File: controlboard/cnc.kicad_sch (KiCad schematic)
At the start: 20 parts, among them J2 LimitSwitch, J3 LimitSwitch, J4 LimitSwitch, J5 LimitSwitch, J6 Electromagnet/Servo, J7 Motor, J8 Motor, Q1 TODO, U2 ????

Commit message: more progress on controlboard pcb
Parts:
- added C6: C_Polarized, symbol Device:C_Polarized
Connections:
- net GND: now also C6.2
- net at JP2.2 (C), JP3.1 (A), Q1.3 (D): now also C6.1
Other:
- note added: "Our motors take 3.7ohm * 1A, 8W, worst case 16 prob + 12V 10 ohms = 1.2A for emag (oof, that's a lot LOT) so let's say 2A for the subsystem VMOT Nom: 10W motor, 6W emag with PWM -> 1.4A"
- note added: "~30 mA / on VIO pins"
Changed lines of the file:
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@@
+	)
+	(junction
+		(at 234.95 73.66)
+		(diameter 0)
+		(color 0 0 0 0)
 	)
 	(junction
@@
 	(wire
 		(pts
-			(xy 232.41 73.66) (xy 240.03 73.66)
+			(xy 232.41 73.66) (xy 234.95 73.66)
 		)
 		(stroke
@@
 	(wire
 		(pts
+			(xy 234.95 73.66) (xy 240.03 73.66)
+		)
+		(stroke
+			(width 0)
+			(type default)
+		)
+	)
+	(wire
+		(pts
 			(xy 87.63 137.16) (xy 90.17 137.16)
 		)
@@
 		(exclude_from_sim no)
 		(at 192.278 65.278 0)
+		(effects
+			(font
+				(size 1.27 1.27)
+			)
+		)
+	)
+	(text "Our motors take 3.7ohm * 1A, 8W, worst case 16 prob\n+ 12V 10 ohms = 1.2A for emag (oof, that's a lot LOT)\n\nso let's say 2A for the subsystem VMOT\n\nNom: 10W motor, 6W emag with PWM -> 1.4A"
+		(exclude_from_sim no)
+		(at 78.232 162.306 0)
+		(effects
+			(font
+				(size 1.27 1.27)
+			)
+		)
+	)
+	(text "~30 mA / on VIO pins\n"
+		(exclude_from_sim no)
+		(at 78.486 154.178 0)
 		(effects
 			(font
@@
 	)
 	(symbol
+		(lib_id "Device:C_Polarized")
+		(at 234.95 77.47 0)
+		(unit 1)
+		(exclude_from_sim no)
+		(in_bom yes)
+		(on_board yes)
+		(dnp no)
+		(property "Reference" "C6"
+			(at 235.712 80.518 0)
+			(effects
+				(font
+					(size 1.27 1.27)
+				)
+				(justify left)
+			)
+		)
+		(property "Value" "C_Polarized"
+			(at 238.76 77.8509 0)
+			(effects
+				(font
+					(size 1.27 1.27)
+				)
+				(justify left)
+				(hide yes)
+			)
+		)
+		(property "Footprint" ""
+			(at 235.9152 81.28 0)
+			(effects
+				(font
+					(size 1.27 1.27)
+				)
+				(hide yes)
+			)
+		)
+		(property "Datasheet" "~"
+			(at 234.95 77.47 0)
+			(effects
+				(font
+					(size 1.27 1.27)
+				)
+				(hide yes)
+			)
+		)
+		(property "Description" "Polarized capacitor"
+			(at 234.95 77.47 0)
+			(effects
+				(font
+					(size 1.27 1.27)
+				)
+				(hide yes)
+			)
+		)
+		(pin "2"
+		)
+		(pin "1"
+		)
+		(instances
+			(project "controlboard"
+				(path "/2797250d-6fee-4769-b4dd-0e20ce4f0941/5be4ea58-2822-4c96-82fa-ac7323f92cc7"
+					(reference "C6")
+					(unit 1)
+				)
+			)
+		)
+	)
+	(symbol
 		(lib_id "power:GND")
 		(at 90.17 90.17 0)
@@
 					(unit 1)
 				)
+			)
+		)
+	)
+	(symbol
+		(lib_id "power:GND")
+		(at 234.95 81.28 0)
+		(unit 1)
+		(exclude_from_sim no)
+		(in_bom yes)
+		(on_board yes)
+		(dnp no)
+		(fields_autoplaced yes)
+		(property "Reference" "#PWR025"
+			(at 234.95 87.63 0)
+			(effects
+				(font
+					(size 1.27 1.27)
+				)
+				(hide yes)
+			)
+		)
+		(property "Value" "GND"
+			(at 234.95 86.36 0)
+			(effects
+				(font
+					(size 1.27 1.27)
+				)
+				(hide yes)
+			)
+		)
+		(property "Footprint" ""
+			(at 234.95 81.28 0)
+			(effects
+				(font
+					(size 1.27 1.27)
+				)
+				(hide yes)
+			)
+		)
+		(property "Datasheet" ""
+			(at 234.95 81.28 0)
+			(effects
+				(font
+					(size 1.27 1.27)
+				)
+				(hide yes)
+			)
+		)
+		(property "Description" ""
+			(at 234.95 81.28 0)
+			(effects
+				(font
+					(size 1.27 1.27)
+				)
+				(hide yes)
+			)
+		)
+		(pin "1"
+		)
+		(instances
+			(project "controlboard"
+				(path "/2797250d-6fee-4769-b4dd-0e20ce4f0941/5be4ea58-2822-4c96-82fa-ac7323f92cc7"
+					(reference "#PWR025")
+					(unit 1)
+				)

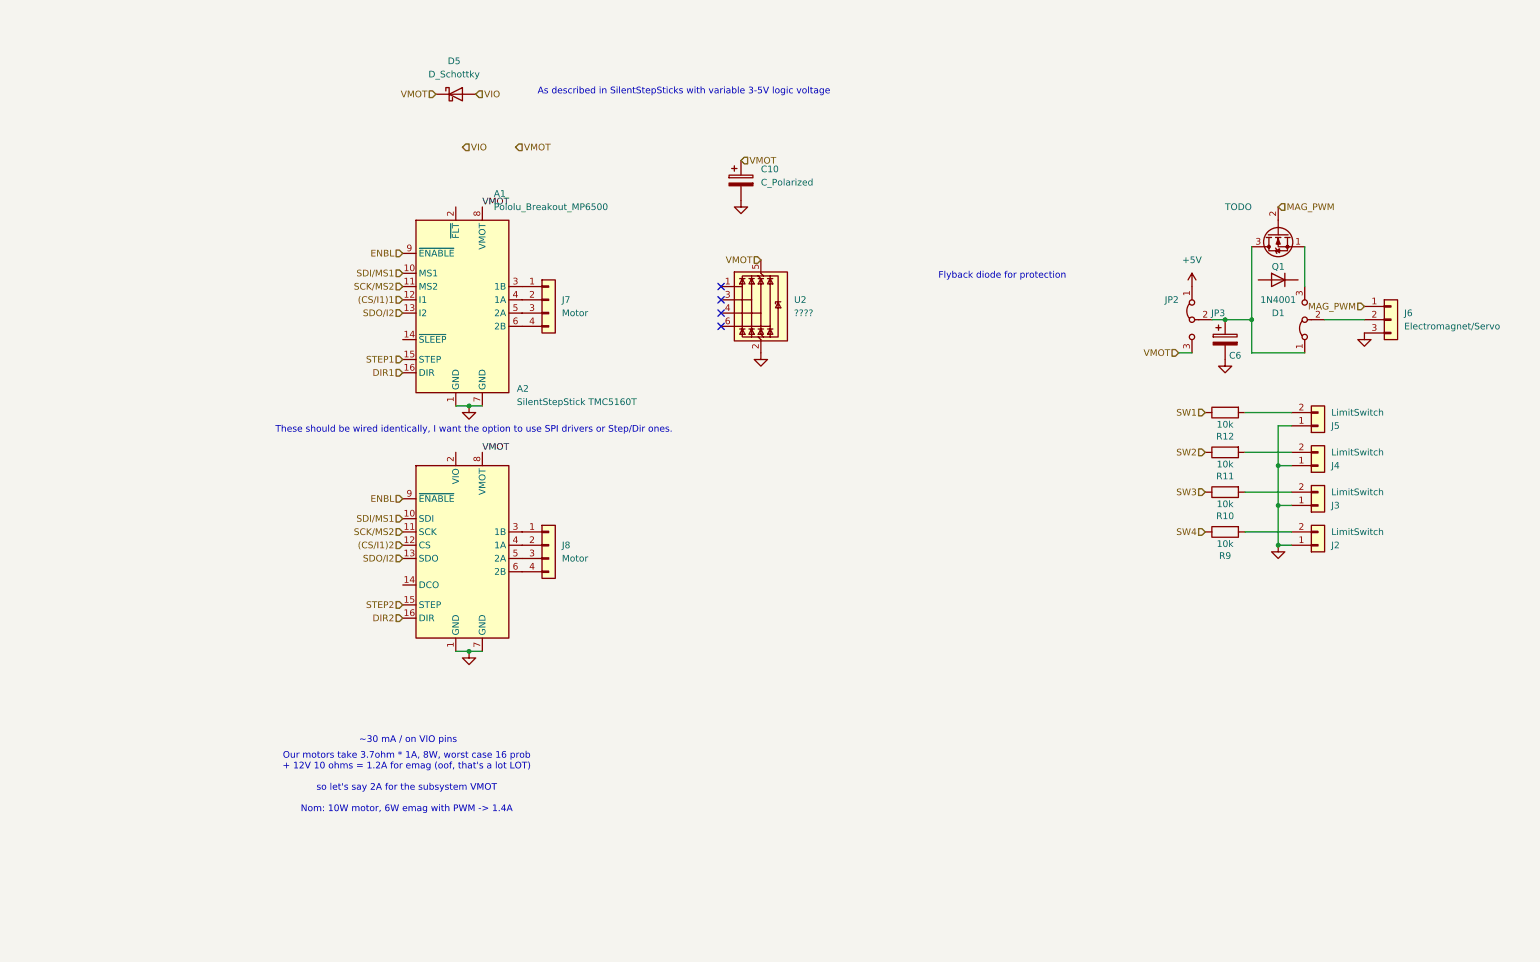
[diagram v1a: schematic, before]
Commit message: ControlBoard Schematic nearly done
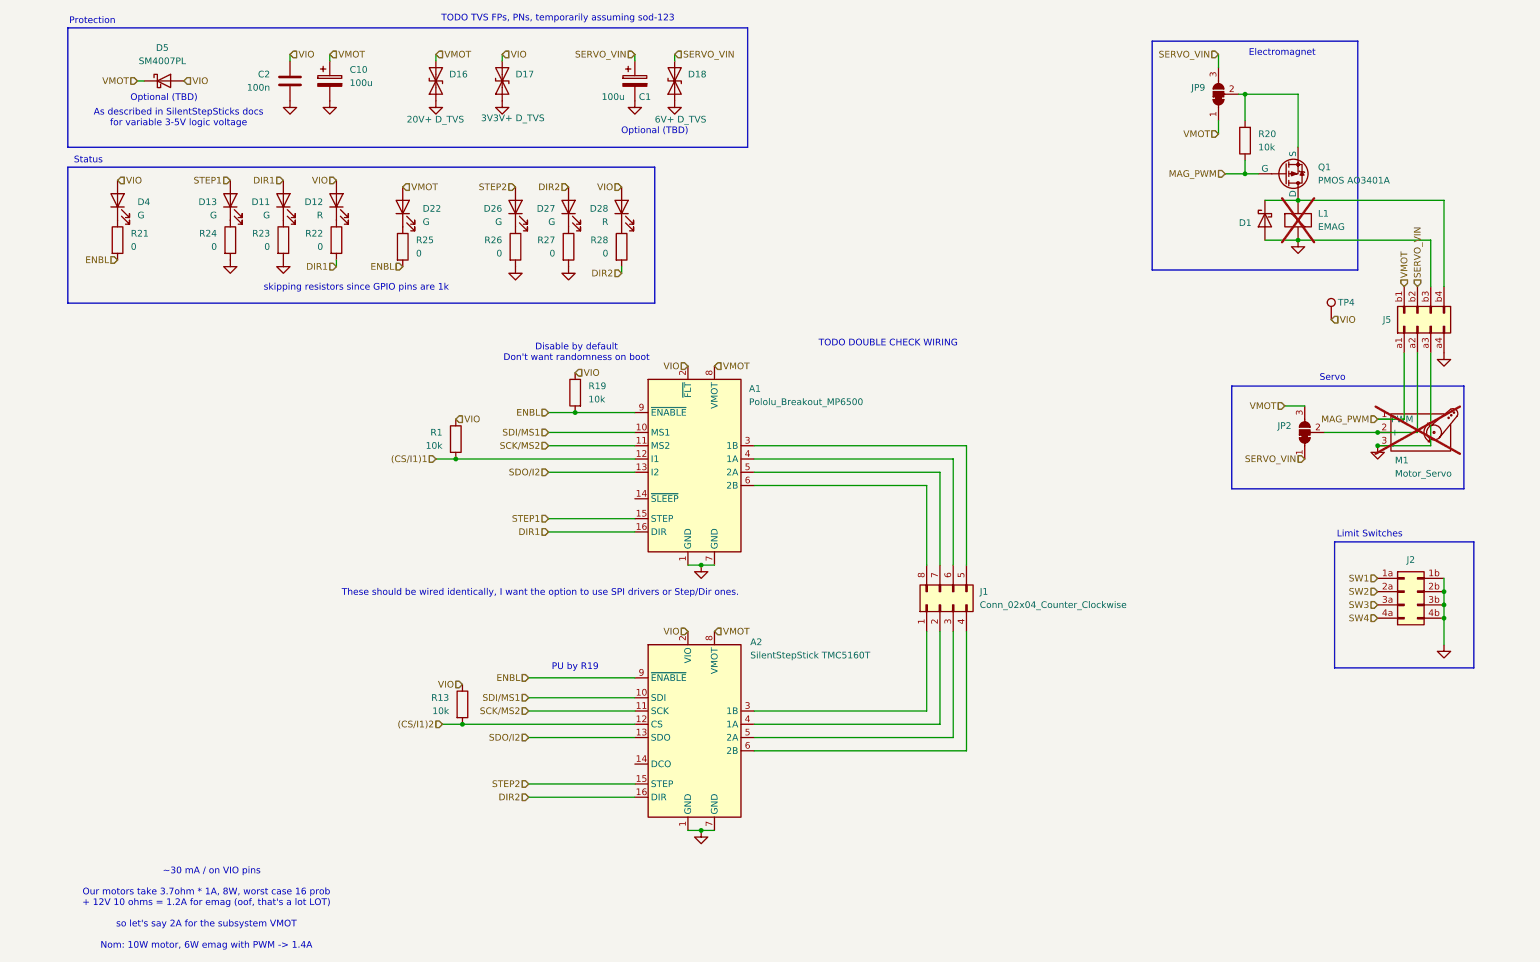
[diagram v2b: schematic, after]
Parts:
- removed C6: C_Polarized, symbol Device:C_Polarized
- removed D1: 1N4001, Diode_THT:D_DO-41_SOD81_P10.16mm_Horizontal, symbol Diode:1N4001
- removed J2, J3, J4, J5: LimitSwitch, symbol Connector_Generic:Conn_01x02
- removed J6: Electromagnet/Servo, symbol Connector_Generic:Conn_01x03
- removed J7, J8: Motor, symbol Connector_Generic:Conn_01x04
- removed JP2, JP3: Jumper_3_Bridged12, symbol Jumper:Jumper_3_Bridged12
- removed Q1: TODO, Package_TO_SOT_THT:TO-92_Inline, symbol Transistor_FET:2N7000
- removed R10, R11, R12, R9: 10k, symbol Device:R
- removed U2: ????, Package_TO_SOT_SMD:SOT-23-6, symbol Power_Protection:WE-TVS-824015043
- added C1: 100u, Capacitor_SMD:CP_Elec_6.3x5.4, symbol Device:C_Polarized
- added C2: 100n, Capacitor_SMD:C_0603_1608Metric_Pad1.08x0.95mm_HandSolder, symbol Device:C
- added D1: SM4007PL, Diode_SMD:Nexperia_CFP3_SOD-123W, symbol Device:D_Schottky
- added D11, D13, D22, D26, D27, D4: G, LED_SMD:LED_0603_1608Metric_Pad1.05x0.95mm_HandSolder, symbol Device:LED
- added D12, D28: R, LED_SMD:LED_0603_1608Metric_Pad1.05x0.95mm_HandSolder, symbol Device:LED
- added D16: 20V+ D_TVS, Diode_SMD:D_SOD-123F, symbol Device:D_TVS
- added D17: 3V3V+ D_TVS, Diode_SMD:D_SOD-123F, symbol Device:D_TVS
- added D18: 6V+ D_TVS, Diode_SMD:D_SOD-123F, symbol Device:D_TVS
- added J1: Conn_02x04_Counter_Clockwise, Connector_PinSocket_2.54mm:PinSocket_2x04_P2.54mm_Horizontal, symbol Connector_Generic:Conn_02x04_Counter_Clockwise
- added J2: Conn_02x04_Row_Letter_Last, Connector_PinSocket_2.54mm:PinSocket_2x04_P2.54mm_Horizontal, symbol Connector_Generic:Conn_02x04_Row_Letter_Last
- added J5: Conn_02x04_Row_Letter_First, Connector_PinSocket_2.54mm:PinSocket_2x04_P2.54mm_Horizontal, symbol Connector_Generic:Conn_02x04_Row_Letter_First
- added JP2, JP9: SolderJumper_3_Bridged12, Jumper:SolderJumper-3_P1.3mm_Bridged12_RoundedPad1.0x1.5mm, symbol Jumper:SolderJumper_3_Bridged12
- added L1: EMAG, symbol Device:ElectromagneticActor
- added M1: Motor_Servo, symbol Motor:Motor_Servo
- added Q1: PMOS AO3401A, Package_TO_SOT_SMD:SOT-23_Handsoldering, symbol Simulation_SPICE:PMOS
- added R1, R13, R19, R20: 10k, Resistor_SMD:R_0603_1608Metric_Pad0.98x0.95mm_HandSolder, symbol Device:R
- added R21, R22, R23, R24, R25, R26, R27, R28: 0, Resistor_SMD:R_0603_1608Metric_Pad0.98x0.95mm_HandSolder, symbol Device:R
- added TP4: TestPoint, Connector_PinSocket_2.54mm:PinSocket_1x01_P2.54mm_Vertical, symbol Connector:TestPoint
- C10: value C_Polarized -> 100u; footprint (none) -> Capacitor_SMD:CP_Elec_6.3x5.4
- D5: value D_Schottky -> SM4007PL; footprint (none) -> Diode_SMD:Nexperia_CFP3_SOD-123W
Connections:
- net (CS/I1)1: now also R1.2
- net (CS/I1)2: now also R13.2
- net DIR1: now also D11.2 (A), R22.2
- net DIR2: now also D27.2 (A), R28.2
- net ENBL: now also R19.2, R21.2, R25.2
- net GND: now also C1.2, C2.2, D1.2 (A), D16.1 (A1), D17.1 (A1), D18.1 (A1), J2.1b (Pin_1b), J2.2b (Pin_2b), J2.3b (Pin_3b), J2.4b (Pin_4b), J5.a3 (Pin_a3), J5.a4 (Pin_a4), J5.b3 (Pin_b3), L1.2 (+), M1.3 (-), R23.2, R24.2, R26.2, R27.2
- net MAG_PWM: now also J5.a1 (Pin_a1), M1.1 (PWM), Q1.2 (G), R20.1
- net STEP1: now also D13.2 (A)
- net STEP2: now also D26.2 (A)
- net SW1: now also J2.1a (Pin_1a)
- net SW2: now also J2.2a (Pin_2a)
- net SW3: now also J2.3a (Pin_3a)
- net SW4: now also J2.4a (Pin_4a)
- net VIO: now also A1.2 (~{FLT}), A2.2 (VIO), C2.1, D12.2 (A), D17.2 (A2), D28.2 (A), D4.2 (A), R1.1, R13.1, R19.1, TP4.1
- net VMOT: now also D16.2 (A2), D22.2 (A), J5.b1 (Pin_b1), JP2.3 (B), JP9.1 (A)
- net at A2.3 (1B): now also J1.1 (Pin_1)
- net at A2.4 (1A): now also J1.2 (Pin_2)
- net at A2.5 (2A): now also J1.3 (Pin_3)
- net at A2.6 (2B): now also J1.4 (Pin_4)
- net at A1.3 (1B): now also J1.5 (Pin_5)
- net at A1.4 (1A): now also J1.6 (Pin_6)
- net at A1.5 (2A): now also J1.7 (Pin_7)
- net at A1.6 (2B): now also J1.8 (Pin_8)
- new net: D26.1 (K), R26.1
- new net: D22.1 (K), R25.1
- new net: D28.1 (K), R28.1
- new net: D13.1 (K), R24.1
- new net: J5.a2 (Pin_a2), JP2.2 (C), M1.2 (+)
- new net: D4.1 (K), R21.1
- new net: D1.1 (K), J5.b4 (Pin_b4), L1.1 (-), Q1.1 (D)
- new net: D12.1 (K), R22.1
- new net: D27.1 (K), R27.1
- new net: JP9.2 (C), Q1.3 (S), R20.2
- new net: D11.1 (K), R23.1
- new net SERVO_VIN: C1.1, D18.2 (A2), J5.b2 (Pin_b2), JP2.1 (A), JP9.3 (B)
- no-connect marks 4 -> 0
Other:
- note added: "As described in SilentStepSticks docs for variable 3-5V logic voltage"
- note added: "Disable by default Don't want randomness on boot"
- note added: "Electromagnet"
- note added: "Limit Switches"
- note added: "Optional (TBD)"
- note added: "PU by R19"
- note added: "Protection"
- note added: "Servo"
- note added: "Status"
- note added: "TODO DOUBLE CHECK WIRING"
- note added: "TODO TVS FPs, PNs, temporarily assuming sod-123"
- note added: "skipping resistors since GPIO pins are 1k"
- note removed: "As described in SilentStepSticks with variable 3-5V logic voltage"
- note removed: "Flyback diode for protection"
- moved on the sheet: A1, A2, C10, D5

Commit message: schematic improvements
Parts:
- removed D22: G, LED_SMD:LED_0603_1608Metric_Pad1.05x0.95mm_HandSolder, symbol Device:LED
- removed R21, R22, R23, R24, R25, R26, R27, R28: 0, Resistor_SMD:R_0603_1608Metric_Pad0.98x0.95mm_HandSolder, symbol Device:R
- D4: value G -> Y
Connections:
- net DIR1: now also D12.1 (K)
- net DIR2: now also D28.1 (K)
- net ENBL: now also D4.1 (K)
- net GND: now also D11.1 (K), D13.1 (K), D26.1 (K), D27.1 (K)
- net VIO: now also J5.b1 (Pin_b1); no longer TP4.1
- net VMOT: now also TP4.1; no longer J5.b1 (Pin_b1)
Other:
- note added: "Assuming sod-123 TVS, will select part numbers later"
- note added: "TODO DOUBLE CHECK THAT PINOUT/SYMBOL/WIRING IS CORRECT FOR MP6500 POLOLU"
- note added: "TODO: Double check that all GPIO pins used by LEDs have resistors (pretty sure they do)"
- note added: "TODO: is this circuit correct"
- note added: "Using software pullups"
- note removed: "TODO DOUBLE CHECK WIRING"
- note removed: "TODO TVS FPs, PNs, temporarily assuming sod-123"

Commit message: erc should be good now
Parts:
- A1: symbol chessbot-parts:Pololu_Breakout_MP6500 -> 0chessbot-parts:Pololu_Breakout_MP6500
- A2: symbol chessbot-parts:SilentStepStick -> 0chessbot-parts:SilentStepStick
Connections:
- no-connect marks 0 -> 2

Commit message: pcb layout work
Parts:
- J2: symbol Connector_Generic:Conn_02x04_Row_Letter_Last -> Connector_Generic:Conn_02x04_Odd_Even
- J5: symbol Connector_Generic:Conn_02x04_Row_Letter_First -> Connector_Generic:Conn_02x04_Odd_Even
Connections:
- net GND: now also J2.2 (Pin_2), J2.4 (Pin_4), J2.6 (Pin_6), J2.8 (Pin_8), J5.5 (Pin_5), J5.6 (Pin_6), J5.7 (Pin_7); no longer J2.1b (Pin_1b), J2.2b (Pin_2b), J2.3b (Pin_3b), J2.4b (Pin_4b), J5.a3 (Pin_a3), J5.a4 (Pin_a4), J5.b3 (Pin_b3)
- net MAG_PWM: now also J5.1 (Pin_1); no longer J5.a1 (Pin_a1)
- net SERVO_VIN: now also J5.4 (Pin_4); no longer J5.b2 (Pin_b2)
- net SW1: now also J2.1 (Pin_1); no longer J2.1a (Pin_1a)
- net SW2: now also J2.3 (Pin_3); no longer J2.2a (Pin_2a)
- net SW3: now also J2.5 (Pin_5); no longer J2.3a (Pin_3a)
- net SW4: now also J2.7 (Pin_7); no longer J2.4a (Pin_4a)
- net VIO: now also J5.2 (Pin_2); no longer J5.b1 (Pin_b1)
- net at JP2.2 (C), M1.2 (+): now also J5.3 (Pin_3); no longer J5.a2 (Pin_a2)
- net at D1.1 (K), L1.1 (-), Q1.1 (D): now also J5.8 (Pin_8); no longer J5.b4 (Pin_b4)

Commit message: progress
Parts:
- removed C1: 100u, Capacitor_SMD:CP_Elec_6.3x5.4, symbol Device:C_Polarized
- removed J1: Conn_02x04_Counter_Clockwise, Connector_PinSocket_2.54mm:PinSocket_2x04_P2.54mm_Horizontal, symbol Connector_Generic:Conn_02x04_Counter_Clockwise
- added C1: 22uF, Capacitor_SMD:C_1206_3216Metric_Pad1.33x1.80mm_HandSolder, symbol Device:C
- added D9: 20V+ D_TVS, Diode_SMD:D_SOD-123F, symbol Device:D_TVS
- added J1: Conn_02x04_Counter_Clockwise, Connector_PinSocket_2.54mm:PinSocket_2x04_P2.54mm_Horizontal, symbol Connector_Generic:Conn_02x04_Odd_Even
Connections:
- net GND: now also C1.2, D9.1 (A1)
- net SERVO_VIN: now also C1.1
- net VMOT: now also D9.2 (A2)
- net at A2.3 (1B): now also J1.2 (Pin_2)
- net at A2.4 (1A): now also J1.4 (Pin_4)
- net at A2.5 (2A): now also J1.6 (Pin_6)
- net at A2.6 (2B): now also J1.8 (Pin_8)
- net at A1.3 (1B): now also J1.1 (Pin_1)
- net at A1.4 (1A): now also J1.3 (Pin_3)
- net at A1.5 (2A): now also J1.5 (Pin_5)
- net at A1.6 (2B): now also J1.7 (Pin_7)
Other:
- moved on the sheet: D11, D12, D13, D26, D27, D28, D4

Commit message: yay its all connected
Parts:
- TP4: footprint Connector_PinSocket_2.54mm:PinSocket_1x01_P2.54mm_Vertical -> TestPoint:TestPoint_THTPad_D2.0mm_Drill1.0mm
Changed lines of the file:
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@@
 			)
 		)
-		(property "Footprint" "Connector_PinSocket_2.54mm:PinSocket_1x01_P2.54mm_Vertical"
+		(property "Footprint" "TestPoint:TestPoint_THTPad_D2.0mm_Drill1.0mm"
 			(at 260.35 73.66 0)
 			(effects

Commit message: a
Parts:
- A1, A2: footprint Module:Pololu_Breakout-16_15.2x20.3mm -> 0chessbot-parts:Pololu_Breakout-16_15.2x20.3mm
- Q1: footprint Package_TO_SOT_SMD:SOT-23_Handsoldering -> Package_TO_SOT_SMD:SOT-23
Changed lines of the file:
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@@
 			)
 		)
-		(property "Footprint" "Module:Pololu_Breakout-16_15.2x20.3mm"
+		(property "Footprint" "0chessbot-parts:Pololu_Breakout-16_15.2x20.3mm"
 			(at 139.065 170.18 0)
 			(effects
@@
 			)
 		)
-		(property "Footprint" "Package_TO_SOT_SMD:SOT-23_Handsoldering"
+		(property "Footprint" "Package_TO_SOT_SMD:SOT-23"
 			(at 251.46 48.26 0)
 			(effects
@@
 			)
 		)
-		(property "Footprint" "Module:Pololu_Breakout-16_15.2x20.3mm"
+		(property "Footprint" "0chessbot-parts:Pololu_Breakout-16_15.2x20.3mm"
 			(at 139.065 119.38 0)
 			(effects
